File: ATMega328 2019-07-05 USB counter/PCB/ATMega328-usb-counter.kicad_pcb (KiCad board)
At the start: 2 copper layers, 56 x 40 mm, 36 parts, among them J1 power, J2 PROG, J3 USB MINI, J4 RF, Q1 MMBT3904, U1 FT230XS, U2 ATmega328PB-AU, U3 74LV8154, X1 ABLNO

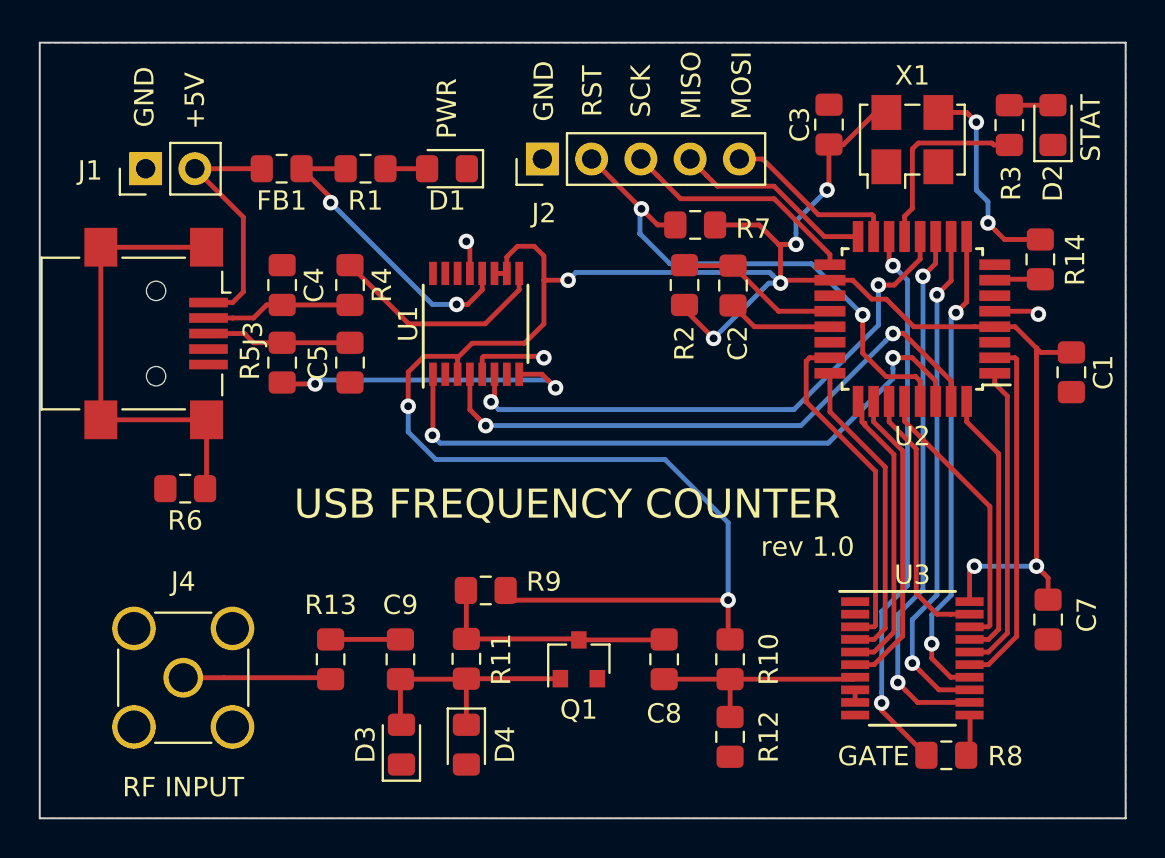
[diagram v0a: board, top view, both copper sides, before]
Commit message: improve PCB
higher impedance front-end, improved silkscreen
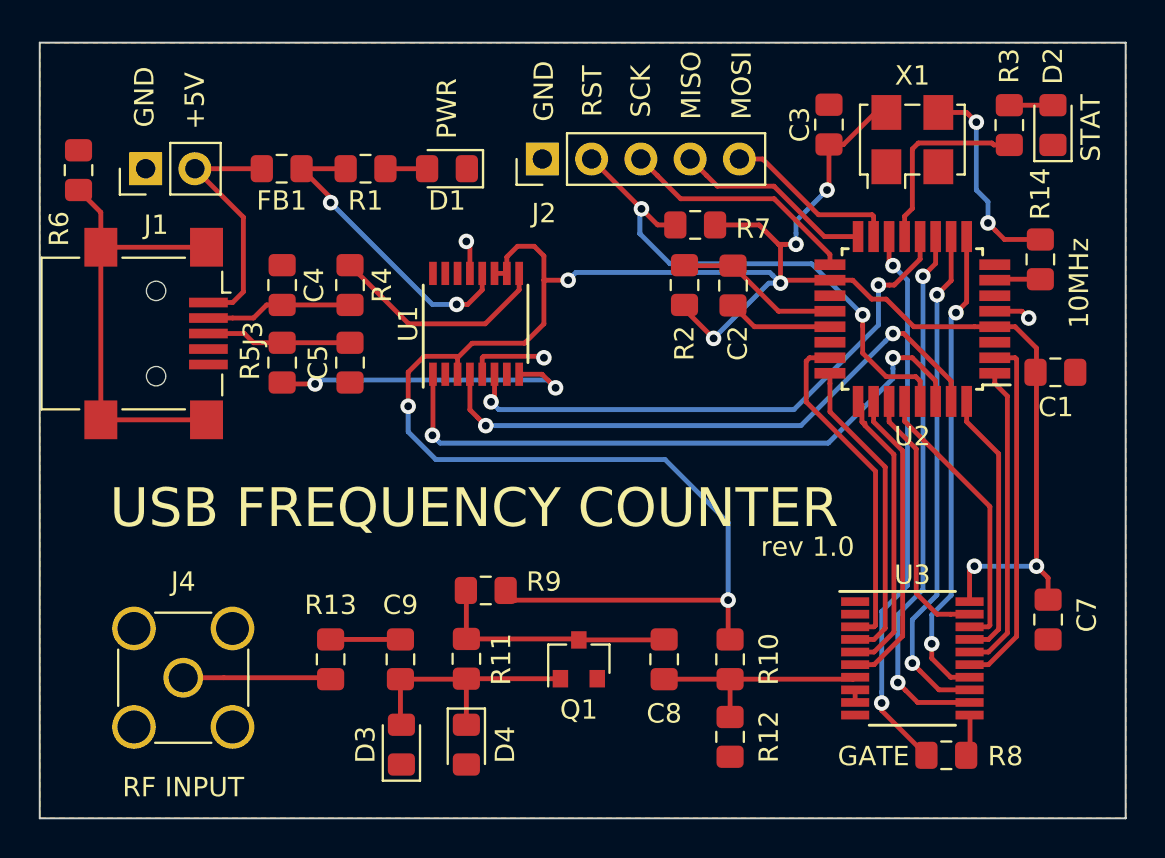
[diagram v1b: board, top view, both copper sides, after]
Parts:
- moved R6 17.3 mm to (60.0, 59.6), turned to 90 degrees
- moved C1 0.83 mm to (110.4, 70.0), turned to 0 degrees
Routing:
- net 3.3V: track 126.9 -> 125.0 mm
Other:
- board text added: "10MHz"
